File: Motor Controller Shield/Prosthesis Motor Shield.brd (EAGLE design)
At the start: 101.6 x 53.3 mm, 46 parts, among them M1_ACT M02PTH, M2_ACT M02PTH

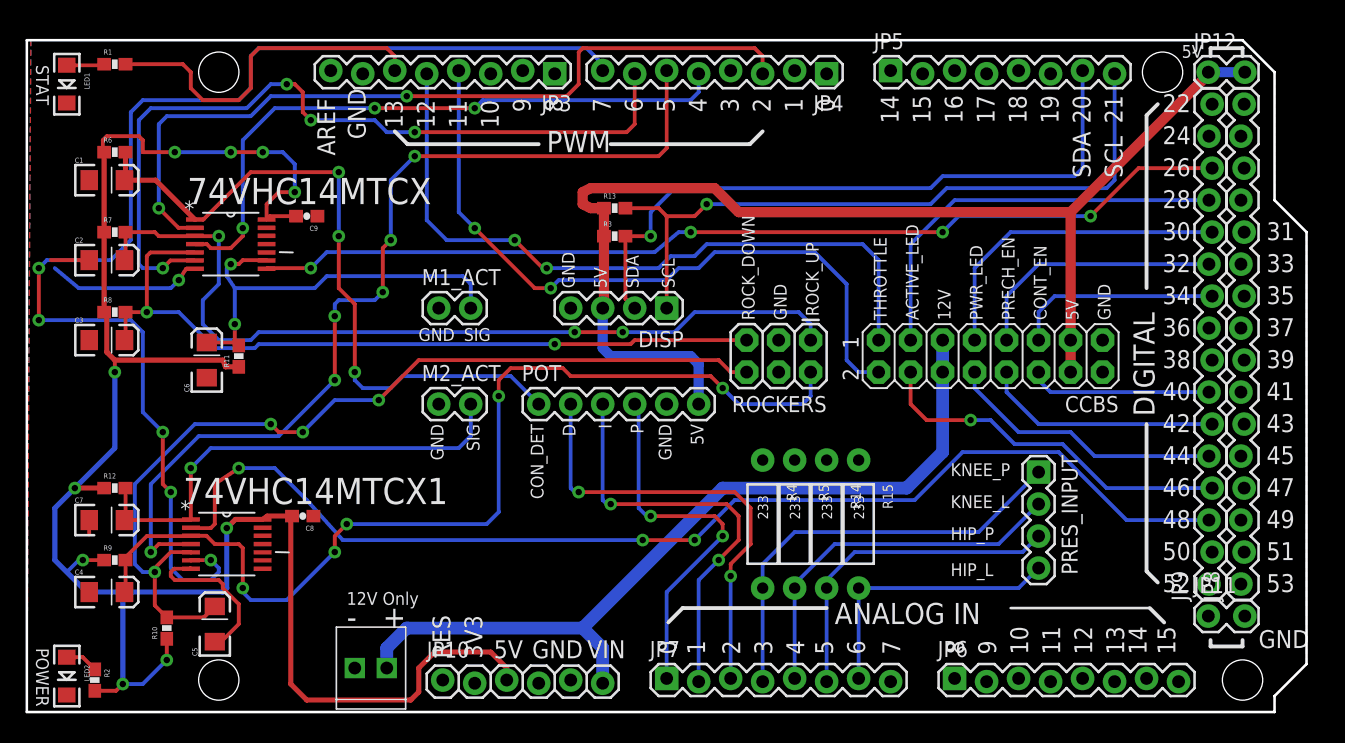
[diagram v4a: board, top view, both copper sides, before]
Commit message: Re-routed motor shield with new molex connectors.
Still may want to put the CCB headers as a better connector, too. Need
to source a good 8x2 pin header first. Added prosthesis logo to motor
board. Added sensor shield schematic (copy of motor board to start)
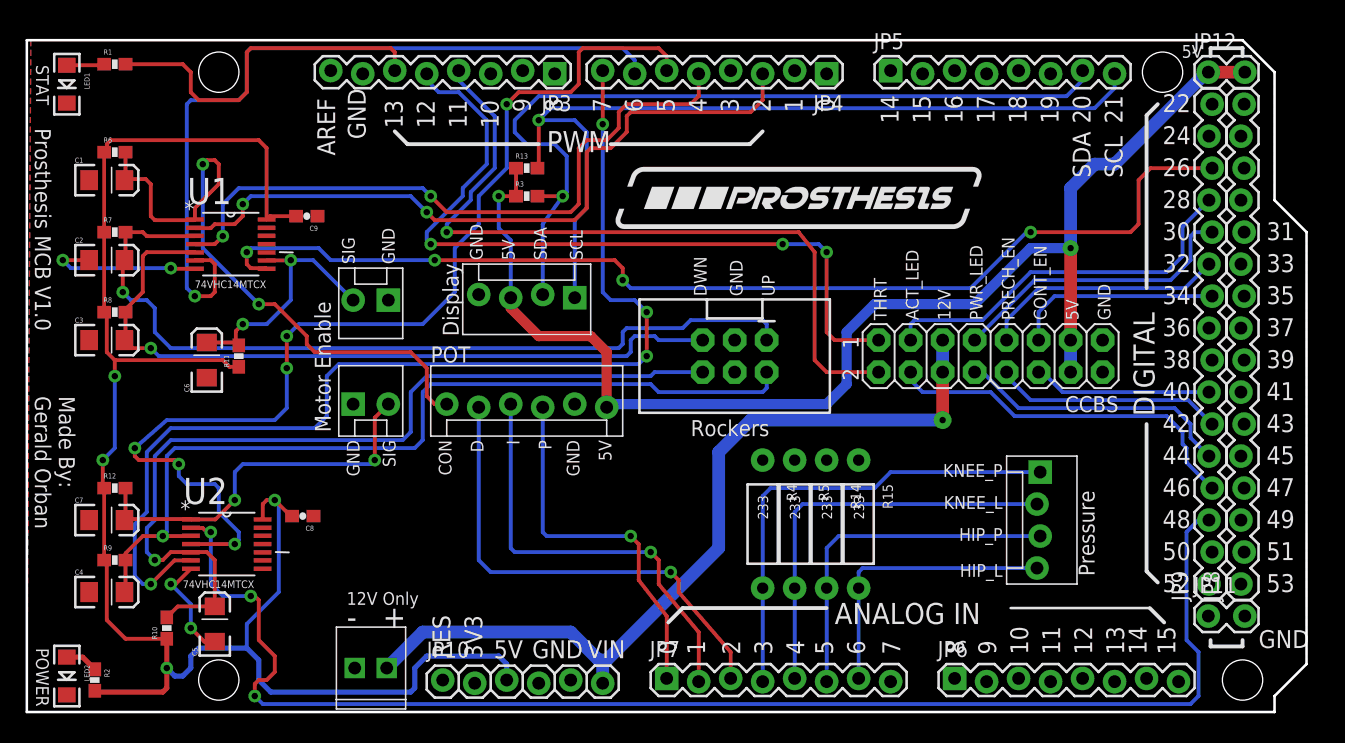
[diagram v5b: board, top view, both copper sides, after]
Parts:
- added U$1: (no value), prosthesis:PROS_LOGO
- C6, C7: value (none) -> 0.1uF
- DISP, PRES_INPUT: device SparkFun-Connectors:1X04 -> SparkFun-Connectors:MOLEX-1X4_LOCK
- M1_ACT, M2_ACT: value M02PTH -> M02POLAR_LOCK; device SparkFun-Connectors:1X02 -> SparkFun-Connectors:MOLEX-1X2_LOCK
- POT: device SparkFun-Connectors:1X06 -> SparkFun-Connectors:MOLEX-1X6_LOCK
- R11, R12: value (none) -> 1M
- ROCKERS: device SparkFun-Connectors:2X3 -> SparkFun-Connectors:2X3-SHROUDED
- moved R3 7.67 mm to (39.7, 41.0)
- moved R13 7.67 mm to (39.7, 43.2)
- moved DISP 7.36 mm to (43.5, 33.0)
- moved POT 7.30 mm to (33.3, 24.4)
- moved M2_ACT 6.67 mm to (26.0, 24.4)
- moved ROCKERS 6.16 mm to (56.2, 28.3), turned to 270 degrees
- moved M1_ACT 4.18 mm to (28.6, 32.7), turned to 180 degrees
- renumbered 74VHC14MTCX to U1, 74VHC14MTCX1 to U2
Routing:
- net D48: track 92.1 -> 110.4 mm
- net 5V: track 153.0 -> 137.1 mm, vias 10 -> 4
- net D7: track 100.2 -> 85.7 mm, vias 5 -> 4
- net M1_ACT_SIG: track 33.8 -> 20.3 mm
- net SCL: track 56.0 -> 69.5 mm
- net SDA: track 53.4 -> 66.7 mm
- net MOT2_ROCK_UP: track 79.9 -> 69.3 mm, vias 5 -> 1
- net D5: track 75.4 -> 85.5 mm
- net D26: track 78.3 -> 87.3 mm
- net GND: track 29.3 -> 21.5 mm, vias 1 -> 4
- net M2_ACT_SIG: track 37.8 -> 30.5 mm, vias 1 -> 2
- net 5V@1: track 96.0 -> 103.0 mm, vias 0 -> 2
- net D2: track 63.8 -> 56.9 mm
- net CON_DET: track 55.3 -> 50.2 mm, vias 3 -> 2
- net D12: track 56.7 -> 61.0 mm, vias 2 -> 3
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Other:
- board text added: "74VHC14MTCX"
- board text added: "ACT_LED"
- board text added: "CON"
- board text added: "DWN"
- board text added: "Display"
- board text added: "Made By: Gerald Orban"
- board text added: "Motor Enable"
- board text added: "Pressure"
- board text added: "Prosthesis MCB V1.0"
- board text added: "Rockers"
- board text added: "THRT"
- board text added: "UP"
- board text removed: "ACTIVE_LED"
- board text removed: "CON_DET"
- board text removed: "ROCK_DOWN"
- board text removed: "ROCK_UP"
- board text removed: "THROTTLE"

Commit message: Moved MCB titles to places layer from names
Cleared sensor shield of all components
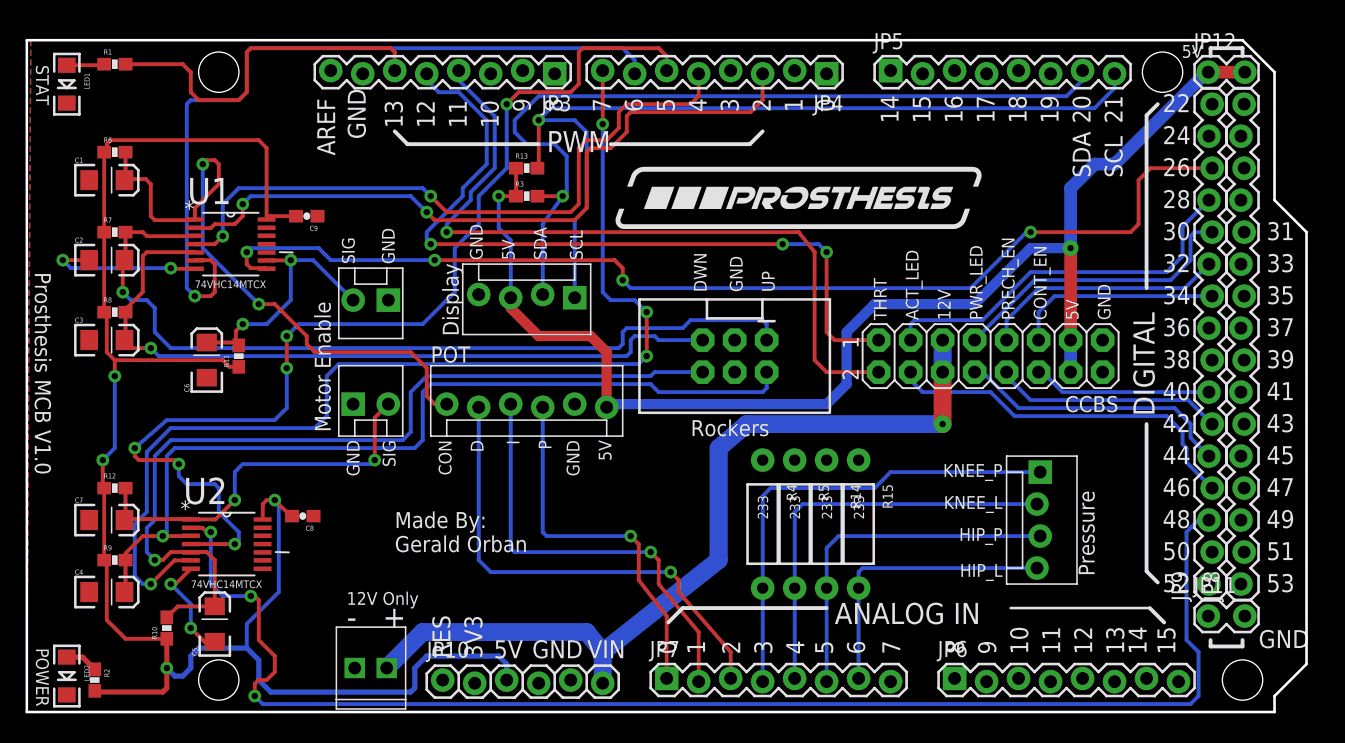
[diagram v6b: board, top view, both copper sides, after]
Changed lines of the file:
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@@
 <layer number="23" name="tOrigins" color="15" fill="1" visible="yes" active="yes"/>
 <layer number="24" name="bOrigins" color="15" fill="1" visible="yes" active="yes"/>
-<layer number="25" name="tNames" color="16" fill="1" visible="yes" active="yes"/>
+<layer number="25" name="tNames" color="16" fill="1" visible="no" active="yes"/>
 <layer number="26" name="bNames" color="7" fill="1" visible="no" active="yes"/>
 <layer number="27" name="tValues" color="7" fill="1" visible="no" active="yes"/>
@@
 <text x="83.5025" y="31.115" size="1.016" layer="21" font="vector" ratio="15" rot="R90">5V</text>
 <text x="68.2625" y="31.115" size="1.016" layer="21" font="vector" ratio="15" rot="R90">THRT</text>
-<text x="59.3725" y="33.02" size="1.016" layer="21" font="vector" ratio="15" rot="R90">UP</text>
-<text x="56.8325" y="33.02" size="1.016" layer="21" font="vector" ratio="15" rot="R90">GND</text>
-<text x="53.975" y="33.02" size="1.016" layer="21" font="vector" ratio="15" rot="R90">DWN</text>
+<text x="59.3725" y="33.3375" size="1.016" layer="21" font="vector" ratio="15" rot="R90">UP</text>
+<text x="56.8325" y="33.3375" size="1.016" layer="21" font="vector" ratio="15" rot="R90">GND</text>
+<text x="53.975" y="33.3375" size="1.016" layer="21" font="vector" ratio="15" rot="R90">DWN</text>
 <text x="77.47" y="19.685" size="1.016" layer="21" font="vector" ratio="15" rot="R180">KNEE_P</text>
 <text x="77.47" y="17.145" size="1.016" layer="21" font="vector" ratio="15" rot="R180">KNEE_L</text>
@@
 <text x="26.035" y="35.56" size="1.016" layer="21" font="vector" ratio="15" rot="R90">SIG</text>
 <text x="28.2575" y="21.59" size="1.016" layer="21" font="vector" ratio="15" rot="R270">SIG</text>
-<text x="13.335" y="33.655" size="0.6096" layer="25" ratio="15">74VHC14MTCX</text>
-<text x="12.3825" y="9.8425" size="0.6096" layer="25" ratio="15">74VHC14MTCX</text>
-<text x="84.7725" y="10.795" size="1.27" layer="25" ratio="15" rot="R90">Pressure</text>
-<text x="52.705" y="21.9075" size="1.27" layer="25" ratio="15">Rockers</text>
-<text x="34.29" y="29.845" size="1.27" layer="25" ratio="15" rot="R90">Display</text>
-<text x="24.13" y="22.225" size="1.27" layer="25" ratio="15" rot="R90">Motor Enable</text>
-<text x="0.635" y="46.355" size="1.27" layer="25" ratio="15" rot="SR270">Prosthesis MCB V1.0</text>
-<text x="0.635" y="25.0825" size="1.27" layer="25" ratio="15" rot="SR270">Made By:
+<text x="13.335" y="33.655" size="0.6096" layer="21" ratio="15">74VHC14MTCX</text>
+<text x="13.0175" y="9.8425" size="0.6096" layer="21" ratio="15">74VHC14MTCX</text>
+<text x="84.7725" y="10.795" size="1.27" layer="21" ratio="15" rot="R90">Pressure</text>
+<text x="52.705" y="21.9075" size="1.27" layer="21" ratio="15">Rockers</text>
+<text x="34.29" y="29.845" size="1.27" layer="21" ratio="15" rot="R90">Display</text>
+<text x="24.13" y="22.225" size="1.27" layer="21" ratio="15" rot="R90">Motor Enable</text>
+<text x="0.635" y="34.925" size="1.27" layer="21" ratio="15" rot="SR270">Prosthesis MCB V1.0</text>
+<text x="29.21" y="12.7" size="1.27" layer="21" ratio="15" rot="SR0">Made By:
 Gerald Orban</text>
 </plain>
@@
 <contactref element="CCBS" pad="11"/>
 <contactref element="CCBS" pad="12"/>
-<wire x1="72.7075" y1="29.5275" x2="72.7075" y2="26.9875" width="1.016" layer="16"/>
-<wire x1="72.7075" y1="26.9875" x2="72.7075" y2="23.1775" width="1.016" layer="1"/>
-<via x="72.7075" y="23.1775" extent="1-16" drill="0.508" diameter="1.4224"/>
-<wire x1="72.7075" y1="23.1775" x2="57.4675" y2="23.1775" width="1.016" layer="16"/>
-<wire x1="57.4675" y1="23.1775" x2="54.9275" y2="20.6375" width="1.016" layer="16"/>
-<wire x1="54.9275" y1="20.6375" x2="54.9275" y2="13.0175" width="1.016" layer="16"/>
-<wire x1="54.9275" y1="13.0175" x2="46.0375" y2="4.1275" width="1.016" layer="16"/>
-<wire x1="46.0375" y1="4.1275" x2="45.72" y2="3.81" width="1.016" layer="16"/>
-<wire x1="45.72" y1="3.81" x2="45.72" y2="2.286" width="1.016" layer="16"/>
-<wire x1="28.575" y1="3.4925" x2="31.4325" y2="6.35" width="1.016" layer="16"/>
-<wire x1="31.4325" y1="6.35" x2="43.18" y2="6.35" width="1.016" layer="16"/>
-<wire x1="43.18" y1="6.35" x2="45.4025" y2="4.1275" width="1.016" layer="16"/>
-<wire x1="45.4025" y1="4.1275" x2="46.0375" y2="4.1275" width="1.016" layer="16"/>
+<wire x1="72.7075" y1="29.5275" x2="72.7075" y2="26.9875" width="1.4224" layer="16"/>
+<wire x1="72.7075" y1="26.9875" x2="72.7075" y2="22.86" width="1.4224" layer="1"/>
+<via x="72.7075" y="22.86" extent="1-16" drill="0.508" diameter="1.4224"/>
+<wire x1="72.7075" y1="22.86" x2="57.15" y2="22.86" width="1.4224" layer="16"/>
+<wire x1="57.15" y1="22.86" x2="54.9275" y2="20.955" width="1.4224" layer="16"/>
+<wire x1="54.9275" y1="20.955" x2="54.9275" y2="12.065" width="1.4224" layer="16"/>
+<wire x1="54.9275" y1="12.065" x2="45.72" y2="4.7625" width="1.4224" layer="16"/>
+<wire x1="45.72" y1="4.7625" x2="45.72" y2="2.286" width="1.4224" layer="16"/>
+<wire x1="28.575" y1="3.4925" x2="31.4325" y2="6.35" width="1.4224" layer="16"/>
+<wire x1="31.4325" y1="6.35" x2="44.45" y2="6.35" width="1.4224" layer="16"/>
+<wire x1="44.45" y1="6.35" x2="45.72" y2="4.7625" width="1.4224" layer="16"/>
 </signal>
 <signal name="A0">

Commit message: CHanged all connectors on MCB to use Molex
Changed most of the connectors on the BMS interface to use molex as
well.
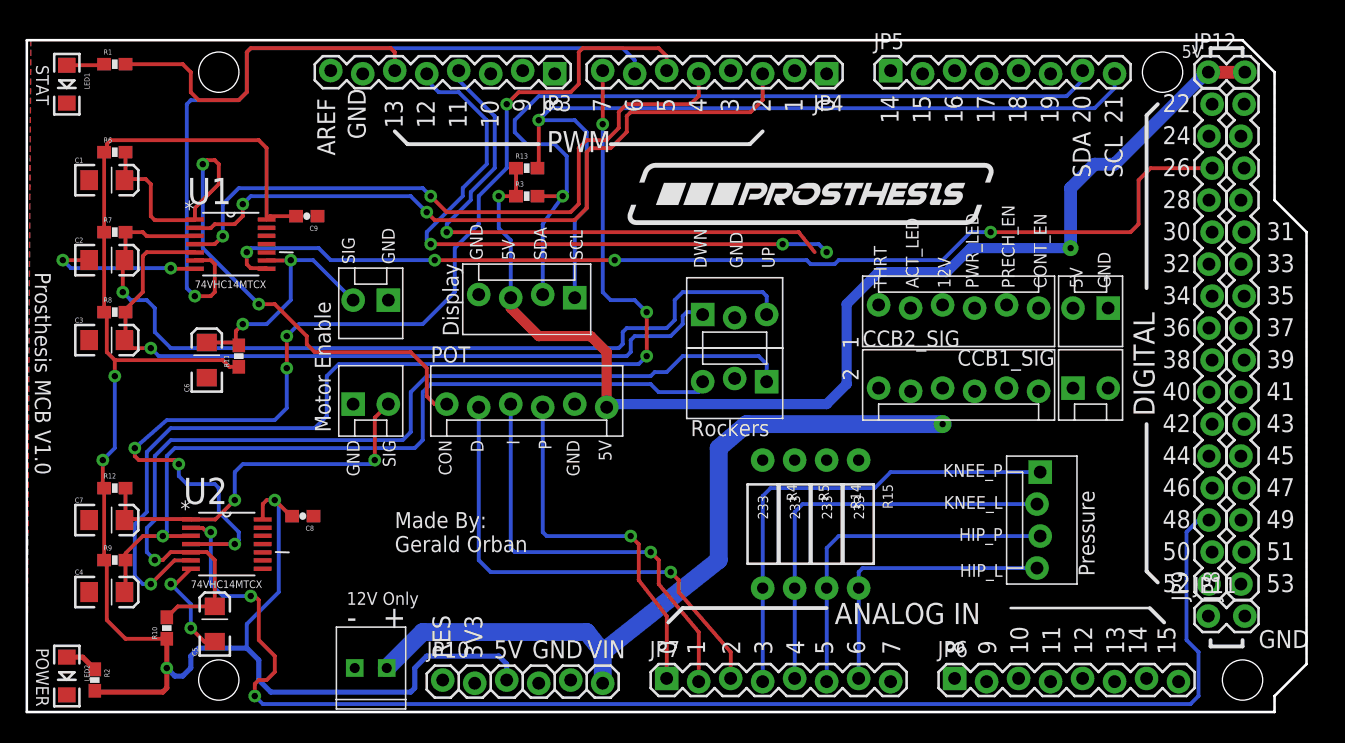
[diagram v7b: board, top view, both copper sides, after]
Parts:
- removed CCBS: M08X2, SparkFun-Connectors:2X8
- removed ROCKERS: (no value), SparkFun-Connectors:2X3-SHROUDED
- added CCB1_PWR, CCB2_PWR: M02POLAR_LOCK, SparkFun-Connectors:MOLEX-1X2_LOCK
- added CCB1_SIG, CCB2_SIG: (no value), SparkFun-Connectors:MOLEX-1X6_LOCK
- added ROCK1, ROCK2: (no value), SparkFun-Connectors:MOLEX-1X3_LOCK
- moved U$1 1.00 mm to (46.0, 37.1)
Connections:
- net 5V@1: now also CCB1_PWR.2, CCB2_PWR.1; no longer CCBS.3, CCBS.4
- net D11: now also CCB2_SIG.1; no longer CCBS.16
- net D12: now also CCB1_SIG.6; no longer CCBS.15
- net D28: now also CCB1_SIG.5; no longer CCBS.13
- net D30: now also CCB1_SIG.3; no longer CCBS.9
- net D32: now also CCB1_SIG.2; no longer CCBS.7
- net D34: now also CCB1_SIG.1; no longer CCBS.5
- net D40: now also CCB2_SIG.6; no longer CCBS.6
- net D42: now also CCB2_SIG.5; no longer CCBS.8
- net D44: now also CCB2_SIG.4; no longer CCBS.10
- net D46: now also CCB2_SIG.2; no longer CCBS.14
- net GND: now also CCB1_PWR.1, CCB2_PWR.2, ROCK1.2, ROCK2.2; no longer CCBS.1, CCBS.2, ROCKERS.3, ROCKERS.4
- net MOT1_ROCK_DOWN: now also ROCK1.1; no longer ROCKERS.5
- net MOT1_ROCK_UP: now also ROCK1.3; no longer ROCKERS.1
- net MOT2_ROCK_DOWN: now also ROCK2.1; no longer ROCKERS.6
- net MOT2_ROCK_UP: now also ROCK2.3; no longer ROCKERS.2
- net VIN: now also CCB1_SIG.4, CCB2_SIG.3; no longer CCBS.11, CCBS.12
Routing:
- net D28: track 30.4 -> 0.00 mm
- net D46: track 29.4 -> 0.00 mm
- net D30: track 23.7 -> 0.00 mm
- net D44: track 22.0 -> 0.00 mm
- net D32: track 19.5 -> 0.00 mm
- net D42: track 18.2 -> 0.00 mm
- net D34: track 16.5 -> 0.00 mm
- net D40: track 14.2 -> 0.00 mm
- net D11: track 59.6 -> 45.6 mm
- net D12: track 61.0 -> 50.2 mm
- net 5V@1: track 103.0 -> 94.4 mm
- net MOT2_ROCK_DOWN: track 70.1 -> 77.3 mm
- net VIN: track 67.4 -> 60.7 mm
- net MOT2_ROCK_UP: track 69.3 -> 63.4 mm
- net D26: track 87.3 -> 85.2 mm
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
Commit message: Missed a save before last commit.
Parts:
- moved ROCK1 0.32 mm to (53.7, 31.8)
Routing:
- net D46: track 0.00 -> 28.6 mm, vias 0 -> 1
- net D28: track 0.00 -> 28.0 mm
- net D30: track 0.00 -> 22.7 mm
- net D44: track 0.00 -> 22.3 mm
- net D42: track 0.00 -> 18.6 mm
- net D32: track 0.00 -> 18.4 mm
- net D34: track 0.00 -> 17.2 mm
- net D40: track 0.00 -> 15.5 mm
- net D11: track 45.6 -> 59.9 mm
- net 5V@1: track 94.4 -> 106.0 mm
- net VIN: track 60.7 -> 69.8 mm, vias 1 -> 0
- net D12: track 50.2 -> 57.6 mm
- net D26: track 85.2 -> 83.1 mm
